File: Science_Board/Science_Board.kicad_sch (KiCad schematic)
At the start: 25 parts, among them J1 Conn_01x02, J10 Conn_01x02, J11 Conn_01x03, J12 Conn_01x03, J13 Conn_01x03, J14 Conn_01x03, J15 Conn_01x03, J16 Conn_01x03, J17 Conn_01x03, J18 Conn_01x03, J19 Conn_01x02, J20 Molex_Megafit_02, J5 Conn_01x02, J6 Conn_01x04, J7 Conn_01x03, J8 Conn_01x03, J9 Conn_01x02, U5 PCA9685BS

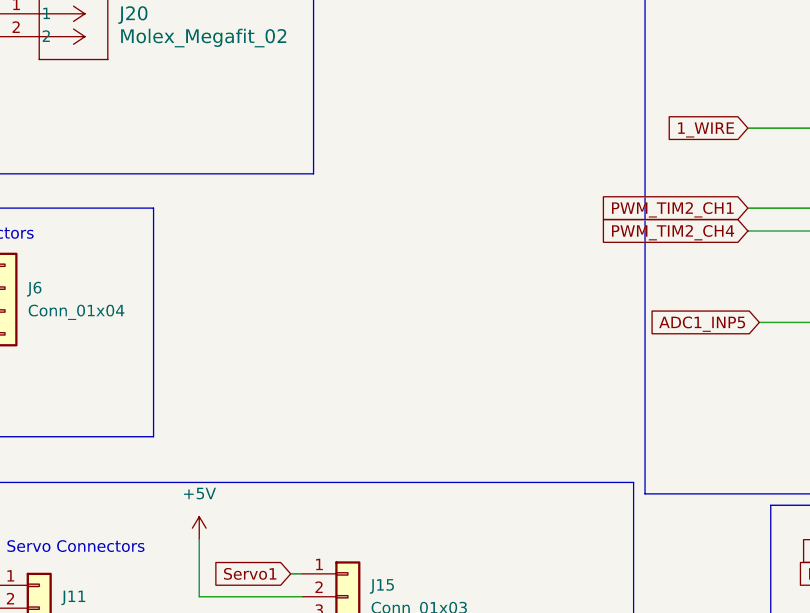
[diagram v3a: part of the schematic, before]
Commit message: added a possible ethernet but may need to check later
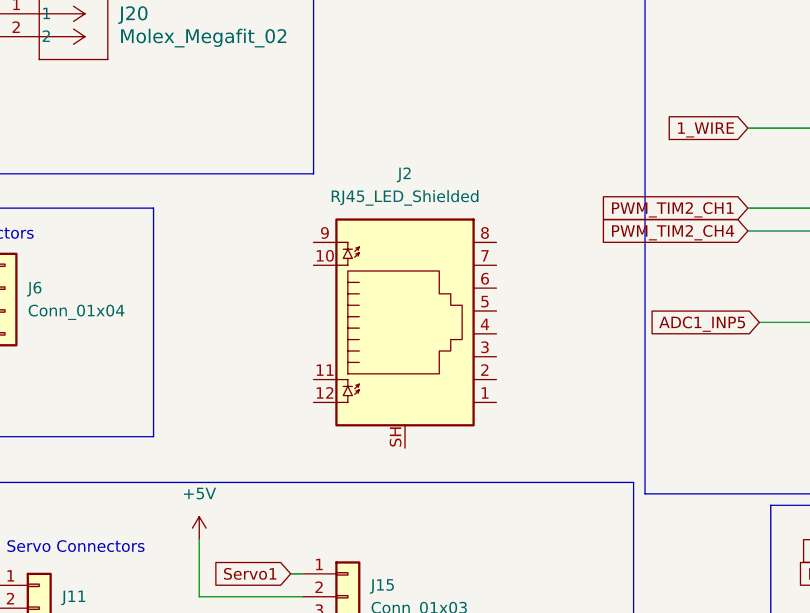
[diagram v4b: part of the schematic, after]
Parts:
- added J2: RJ45_LED_Shielded, Connector_RJ:RJ45_Amphenol_RJMG1BD3B8K1ANR, symbol Connector:RJ45_LED_Shielded
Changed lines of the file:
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@@
+	)
+	(symbol
+		(lib_id "Connector:RJ45_LED_Shielded")
+		(at 80.01 74.93 0)
+		(unit 1)
+		(body_style 1)
+		(exclude_from_sim no)
+		(in_bom yes)
+		(on_board yes)
+		(in_pos_files yes)
+		(dnp no)
+		(fields_autoplaced yes)
+		(property "Reference" "J2"
+			(at 80.01 57.15 0)
+			(show_name no)
+			(do_not_autoplace no)
+			(effects
+				(font
+					(size 1.27 1.27)
+				)
+			)
+		)
+		(property "Value" "RJ45_LED_Shielded"
+			(at 80.01 59.69 0)
+			(show_name no)
+			(do_not_autoplace no)
+			(effects
+				(font
+					(size 1.27 1.27)
+				)
+			)
+		)
+		(property "Footprint" "Connector_RJ:RJ45_Amphenol_RJMG1BD3B8K1ANR"
+			(at 80.01 74.295 90)
+			(hide yes)
+			(show_name no)
+			(do_not_autoplace no)
+			(effects
+				(font
+					(size 1.27 1.27)
+				)
+			)
+		)
+		(property "Datasheet" ""
+			(at 80.01 74.295 90)
+			(hide yes)
+			(show_name no)
+			(do_not_autoplace no)
+			(effects
+				(font
+					(size 1.27 1.27)
+				)
+			)
+		)
+		(property "Description" "RJ connector, 8P8C (8 positions 8 connected), two LEDs, Shielded"
+			(at 80.01 74.93 0)
+			(hide yes)
+			(show_name no)
+			(do_not_autoplace no)
+			(effects
+				(font
+					(size 1.27 1.27)
+				)
+			)
+		)
+		(pin "7"
+		)
+		(pin "11"
+		)
+		(pin "8"
+		)
+		(pin "12"
+		)
+		(pin "1"
+		)
+		(pin "2"
+		)
+		(pin "9"
+		)
+		(pin "10"
+		)
+		(pin "SH"
+		)
+		(pin "6"
+		)
+		(pin "4"
+		)
+		(pin "3"
+		)
+		(pin "5"
+		)
+		(instances
+			(project "Science_Board"
+				(path "/4f5c5f7f-4385-4de2-96ca-2ae741ebf691"
+					(reference "J2")
+					(unit 1)
+				)
+			)
+		)
 	)
 	(symbol

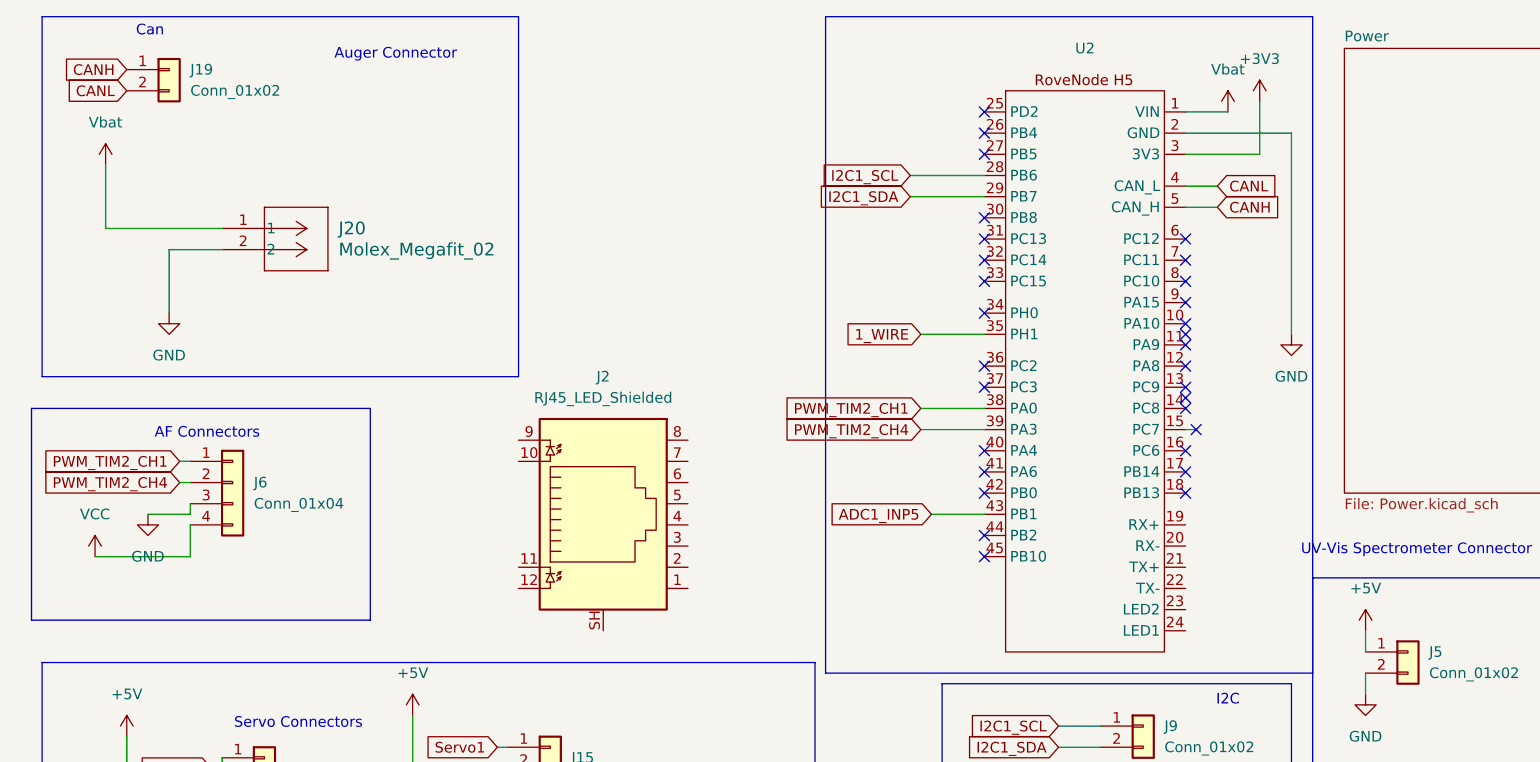
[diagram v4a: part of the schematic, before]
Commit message: fuse trip
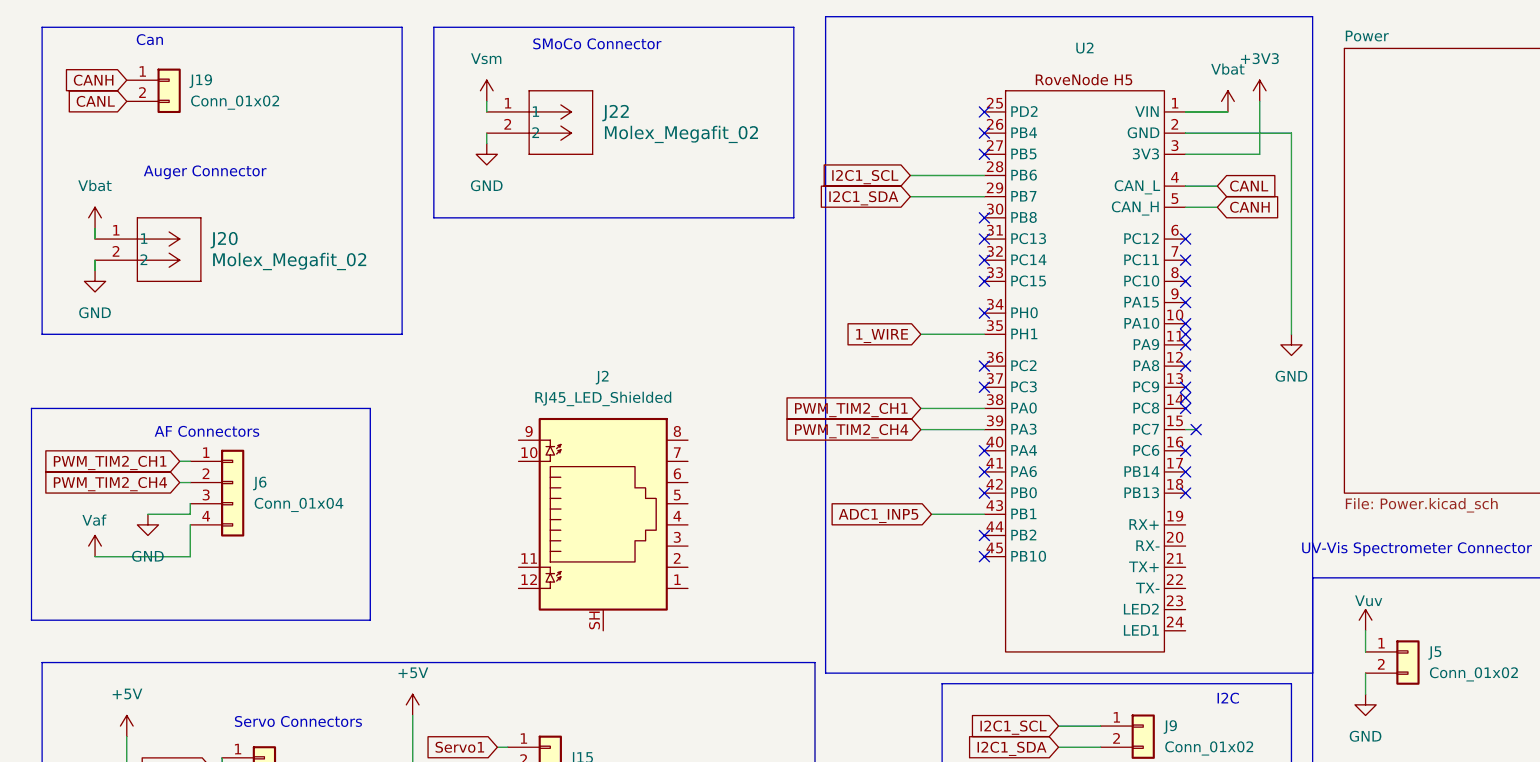
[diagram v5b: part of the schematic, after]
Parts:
- added J22: Molex_Megafit_02, MRDT_Connectors:MOLEX_MegaFit_02_Horizontal, symbol MRDT_Connectors:Molex_Megafit_02
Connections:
- net +5V: no longer J5.1 (Pin_1)
- net GND: now also J22.2
- net VCC: no longer J6.4 (Pin_4)
- new net Vaf: J6.4 (Pin_4)
- new net Vsm: J22.1
- new net Vuv: J5.1 (Pin_1)
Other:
- note added: "SMoCo Connector"

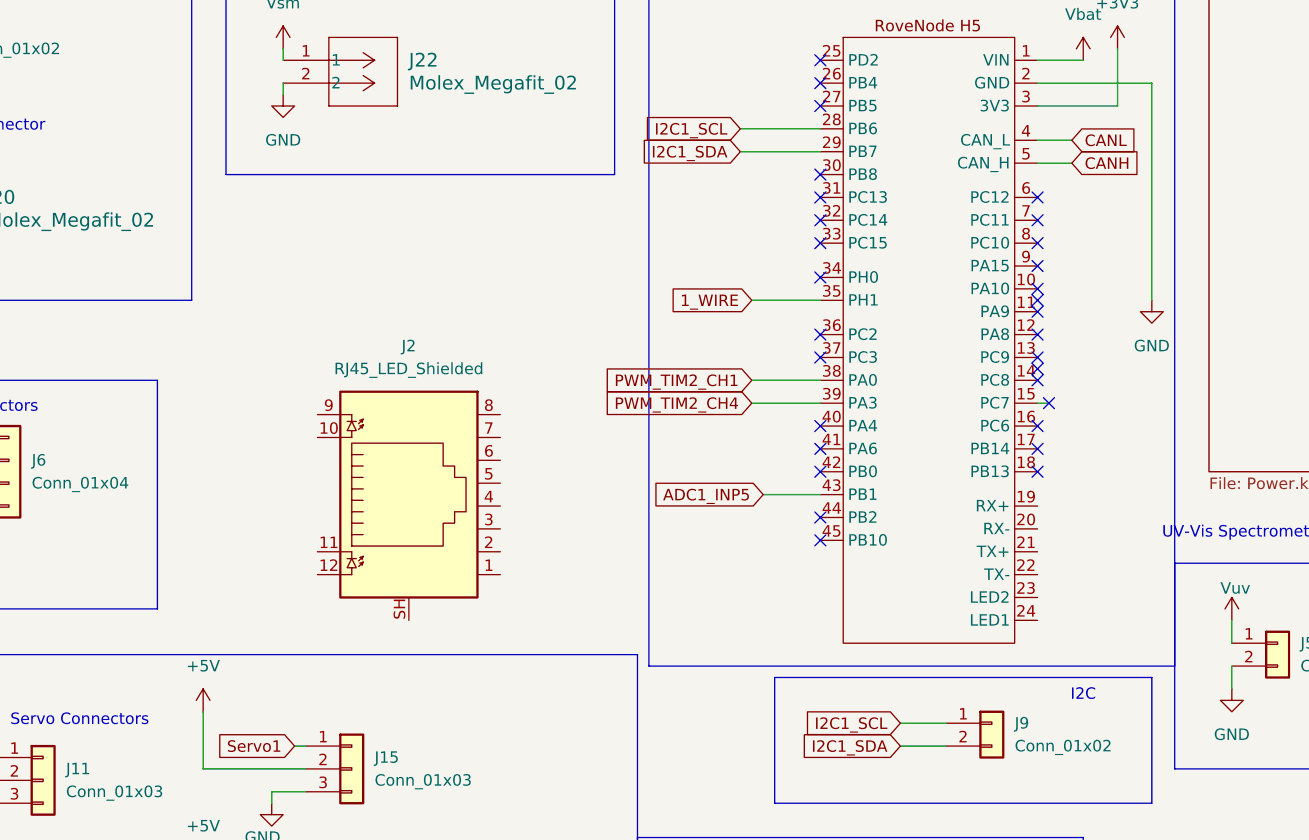
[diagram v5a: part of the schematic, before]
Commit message: Added RJ45 Connector
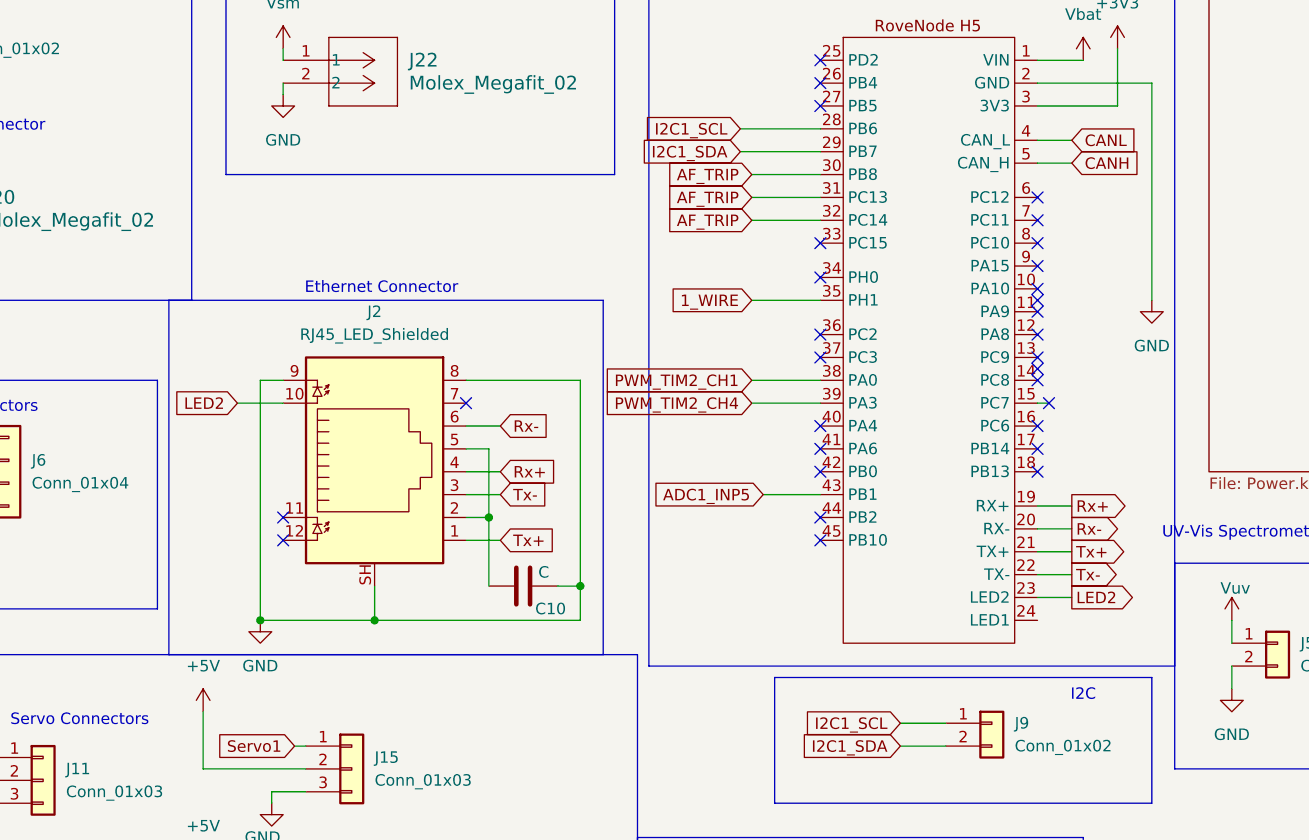
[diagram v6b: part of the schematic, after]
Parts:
- added C10: C, symbol Device:C
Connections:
- net GND: now also J2.8, J2.9, J2.SH, C10.2
- net Tx+: now reaches J2.1
- net Tx+: now also U2.21 (TX+)
- net LED2: now reaches J2.10
- net LED2: now also U2.23 (LED2)
- net at J2.2: now also J2.5, C10.1
- net Tx-: now reaches J2.3
- net Tx-: now also U2.22 (TX-)
- net Rx+: now reaches J2.4
- net Rx+: now also U2.19 (RX+)
- net Rx-: now reaches J2.6
- net Rx-: now also U2.20 (RX-)
- net AF_TRIP: now reaches U2.30 (PB8)
- net AF_TRIP: now also U2.31 (PC13), U2.32 (PC14)
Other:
- note added: "Ethernet Connector"
- moved on the sheet: J2

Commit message: Add Footprints
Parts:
- C10: value C -> .1uF; footprint (none) -> Capacitor_SMD:C_0201_0603Metric_Pad0.64x0.40mm_HandSolder
- D2, D3, D4: footprint (none) -> Diode_SMD:D_0603_1608Metric_Pad1.05x0.95mm_HandSolder
- J1: footprint (none) -> Connector_JST:JST_PH_B2B-PH-K_1x02_P2.00mm_Vertical
- J10, J5, J9: footprint Package_DFN_QFN:QFN-20-1EP_5x5mm_P0.65mm_EP3.35x3.35mm -> Connector_JST:JST_PH_B2B-PH-K_1x02_P2.00mm_Vertical
- J11, J7, J8: footprint Package_DFN_QFN:QFN-20-1EP_5x5mm_P0.65mm_EP3.35x3.35mm -> Connector_JST:JST_PH_B3B-PH-K_1x03_P2.00mm_Vertical
- J12, J13, J14, J15, J16, J17, J18, J19: footprint (none) -> Connector_JST:JST_PH_B3B-PH-K_1x03_P2.00mm_Vertical
- J6: footprint Package_DFN_QFN:QFN-20-1EP_5x5mm_P0.65mm_EP3.35x3.35mm -> Connector_JST:JST_PH_B4B-PH-K_1x04_P2.00mm_Vertical
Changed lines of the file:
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@@
 	(text "UV-Vis Spectrometer Connector"
 		(exclude_from_sim no)
-		(at 177.546 77.978 0)
+		(at 180.594 79.248 0)
 		(effects
 			(font
@@
 	)
 	(global_label "Rx-"
-		(shape input)
+		(shape output)
 		(at 90.17 66.04 0)
 		(fields_autoplaced yes)
@@
 	)
 	(global_label "Rx-"
-		(shape output)
+		(shape input)
 		(at 153.67 77.47 0)
 		(fields_autoplaced yes)
@@
 	)
 	(global_label "Rx+"
-		(shape output)
+		(shape input)
 		(at 153.67 74.93 0)
 		(fields_autoplaced yes)
@@
 	)
 	(global_label "Rx+"
-		(shape input)
+		(shape output)
 		(at 90.17 71.12 0)
 		(fields_autoplaced yes)
@@
 			)
 		)
-		(property "Value" "C"
-			(at 94.996 82.296 90)
+		(property "Value" ".1uF"
+			(at 96.266 82.55 90)
 			(show_name no)
 			(do_not_autoplace no)
@@
 			)
 		)
-		(property "Footprint" ""
+		(property "Footprint" "Capacitor_SMD:C_0201_0603Metric_Pad0.64x0.40mm_HandSolder"
 			(at 96.52 82.8548 0)
 			(hide yes)
@@
 			)
 		)
-		(property "Footprint" ""
+		(property "Footprint" "Diode_SMD:D_0603_1608Metric_Pad1.05x0.95mm_HandSolder"
 			(at 240.03 36.83 0)
 			(hide yes)
@@
 			)
 		)
-		(property "Footprint" ""
+		(property "Footprint" "Diode_SMD:D_0603_1608Metric_Pad1.05x0.95mm_HandSolder"
 			(at 271.78 36.83 0)
 			(hide yes)
@@
 			)
 		)
-		(property "Footprint" ""
+		(property "Footprint" "Connector_JST:JST_PH_B3B-PH-K_1x03_P2.00mm_Vertical"
 			(at 40.64 116.84 0)
 			(hide yes)
@@
 			)
 		)
-		(property "Footprint" ""
+		(property "Footprint" "Connector_JST:JST_PH_B3B-PH-K_1x03_P2.00mm_Vertical"
 			(at 73.66 104.14 0)
 			(hide yes)
@@
 			)
 		)
-		(property "Footprint" "Package_DFN_QFN:QFN-20-1EP_5x5mm_P0.65mm_EP3.35x3.35mm"
+		(property "Footprint" "Connector_JST:JST_PH_B3B-PH-K_1x03_P2.00mm_Vertical"
 			(at 137.16 125.73 0)
 			(hide yes)
@@
 			)
 		)
-		(property "Footprint" ""
+		(property "Footprint" "Connector_JST:JST_PH_B2B-PH-K_1x02_P2.00mm_Vertical"
 			(at 36.83 181.61 0)
 			(hide yes)
@@
 			)
 		)
-		(property "Footprint" ""
+		(property "Footprint" "Connector_JST:JST_PH_B3B-PH-K_1x03_P2.00mm_Vertical"
 			(at 39.37 137.16 0)
 			(hide yes)
@@
 			)
 		)
-		(property "Footprint" ""
+		(property "Footprint" "Connector_JST:JST_PH_B3B-PH-K_1x03_P2.00mm_Vertical"
 			(at 74.93 129.54 0)
 			(hide yes)
@@
 			)
 		)
-		(property "Footprint" "Package_DFN_QFN:QFN-20-1EP_5x5mm_P0.65mm_EP3.35x3.35mm"
+		(property "Footprint" "Connector_JST:JST_PH_B4B-PH-K_1x04_P2.00mm_Vertical"
 			(at 35.56 69.85 0)
 			(hide yes)
@@
 			)
 		)
-		(property "Footprint" "Package_DFN_QFN:QFN-20-1EP_5x5mm_P0.65mm_EP3.35x3.35mm"
+		(property "Footprint" "Connector_JST:JST_PH_B2B-PH-K_1x02_P2.00mm_Vertical"
 			(at 176.53 128.27 0)
 			(hide yes)
@@
 			)
 		)
-		(property "Footprint" "Package_DFN_QFN:QFN-20-1EP_5x5mm_P0.65mm_EP3.35x3.35mm"
+		(property "Footprint" "Connector_JST:JST_PH_B3B-PH-K_1x03_P2.00mm_Vertical"
 			(at 157.48 163.83 0)
 			(hide yes)
@@
 			)
 		)
-		(property "Footprint" ""
+		(property "Footprint" "Diode_SMD:D_0603_1608Metric_Pad1.05x0.95mm_HandSolder"
 			(at 259.08 36.83 0)
 			(hide yes)
@@
 			)
 		)
-		(property "Footprint" ""
+		(property "Footprint" "Connector_JST:JST_PH_B3B-PH-K_1x03_P2.00mm_Vertical"
 			(at 74.93 116.84 0)
 			(hide yes)
@@
 			)
 		)
-		(property "Footprint" "Package_DFN_QFN:QFN-20-1EP_5x5mm_P0.65mm_EP3.35x3.35mm"
+		(property "Footprint" "Connector_JST:JST_PH_B3B-PH-K_1x03_P2.00mm_Vertical"
 			(at 39.37 105.41 0)
 			(hide yes)
@@
 			)
 		)
-		(property "Footprint" "Package_DFN_QFN:QFN-20-1EP_5x5mm_P0.65mm_EP3.35x3.35mm"
+		(property "Footprint" "Connector_JST:JST_PH_B2B-PH-K_1x02_P2.00mm_Vertical"
 			(at 176.53 90.17 0)
 			(hide yes)
@@
 			)
 		)
-		(property "Footprint" ""
+		(property "Footprint" "Connector_JST:JST_PH_B3B-PH-K_1x03_P2.00mm_Vertical"
 			(at 45.72 162.56 0)
 			(hide yes)
@@
 			)
 		)
-		(property "Footprint" "Package_DFN_QFN:QFN-20-1EP_5x5mm_P0.65mm_EP3.35x3.35mm"
+		(property "Footprint" "Connector_JST:JST_PH_B2B-PH-K_1x02_P2.00mm_Vertical"
 			(at 144.78 99.06 0)
 			(hide yes)
@@
 			)
 		)
-		(property "Footprint" ""
+		(property "Footprint" "Connector_JST:JST_PH_B3B-PH-K_1x03_P2.00mm_Vertical"
 			(at 27.94 21.59 0)
 			(hide yes)
@@
 			)
 		)
-		(property "Footprint" ""
+		(property "Footprint" "Connector_JST:JST_PH_B3B-PH-K_1x03_P2.00mm_Vertical"
 			(at 91.44 163.83 0)
 			(hide yes)

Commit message: Added mounting holes
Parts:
- added H1, H2, H3, H4: MountingHole, symbol Mechanical:MountingHole
